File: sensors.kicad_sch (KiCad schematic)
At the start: 13 parts, among them U5 LIS2MDL, U6 SAM-M10Q

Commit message: modified BOM
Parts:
- C13, C17: Distributor Link https://www.lcsc.com/product-detail/C95841.html -> https://www.digikey.com/en/products/detail/samsung-electro-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
- C14, C15, C18, C23: Distributor Link https://www.lcsc.com/product-detail/C519980.html -> https://www.digikey.com/en/products/detail/samsung-electro-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; MPN CC0805KRX7R7BB104 -> CL21B104KBCNNNC; Manufacturer YAGEO -> Samsung Electro-Mechanics
- C16: Distributor Link https://www.lcsc.com/product-detail/C113853.html -> https://www.digikey.com/en/products/detail/samsung-electro-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; MPN CC0805KRX7R7BB224 -> CL21B224KAFNNNE; Manufacturer YAGEO -> Samsung Electro-Mechanics
- R14, R15: Distributor Link https://www.lcsc.com/product-detail/C17414.html -> https://www.digikey.com/en/products/detail/yageo/RC0805JR-0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; MPN 0805W8F1002T5E -> RC0805JR-0710KL; Manufacturer UNI-ROYAL -> YAGEO
- R16, R17: Distributor Link https://www.lcsc.com/product-detail/C17520.html -> https://www.digikey.com/en/products/detail/yageo/RC0805FR-0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; MPN 0805W8F2201T5E -> RC0805FR-072K2L; Manufacturer UNI-ROYAL -> YAGEO
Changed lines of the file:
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@@
 			)
 		)
-		(property "Datasheet" "https://www.lcsc.com/datasheet/C519980.pdf"
+		(property "Datasheet" ""
 			(at 182.88 59.69 0)
 			(effects
@@
 			)
 		)
-		(property "MPN" "CC0805KRX7R7BB104"
+		(property "MPN" "CL21B104KBCNNNC"
 			(at 182.88 59.69 0)
 			(effects
@@
 			)
 		)
-		(property "Manufacturer" "YAGEO"
+		(property "Manufacturer" "Samsung Electro-Mechanics"
 			(at 182.88 59.69 0)
 			(effects
@@
 			)
 		)
-		(property "Distributor Link" "https://www.lcsc.com/product-detail/C519980.html"
+		(property "Distributor Link" "https://www.digikey.com/en/products/detail/samsung-electro-mechanics/CL21B104KBCNNNC/3886661"
+			(at 182.88 59.69 0)
+			(effects
+				(font
+					(size 1.27 1.27)
+				)
+				(hide yes)
+			)
+		)
+		(property "DIGIKEY" ""
 			(at 182.88 59.69 0)
 			(effects
@@
 			)
 		)
+		(property "DIGIKEY" ""
+			(at 96.52 82.55 0)
+			(effects
+				(font
+					(size 1.27 1.27)
+				)
+				(hide yes)
+			)
+		)
 		(pin "3"
 		)
@@
 			)
 		)
-		(property "Datasheet" "https://www.lcsc.com/datasheet/C113853.pdf"
+		(property "Datasheet" ""
 			(at 119.38 92.71 0)
 			(effects
@@
 			)
 		)
-		(property "MPN" "CC0805KRX7R7BB224"
+		(property "MPN" "CL21B224KAFNNNE"
 			(at 119.38 92.71 0)
 			(effects
@@
 			)
 		)
-		(property "Manufacturer" "YAGEO"
+		(property "Manufacturer" "Samsung Electro-Mechanics"
 			(at 119.38 92.71 0)
 			(effects
@@
 			)
 		)
-		(property "Distributor Link" "https://www.lcsc.com/product-detail/C113853.html"
+		(property "Distributor Link" "https://www.digikey.com/en/products/detail/samsung-electro-mechanics/CL21B224KAFNNNE/3886819"
+			(at 119.38 92.71 0)
+			(effects
+				(font
+					(size 1.27 1.27)
+				)
+				(hide yes)
+			)
+		)
+		(property "DIGIKEY" ""
 			(at 119.38 92.71 0)
 			(effects
@@
 			)
 		)
-		(property "Datasheet" "https://www.lcsc.com/datasheet/C17520.pdf"
+		(property "Datasheet" ""
 			(at 218.44 78.74 0)
 			(effects
@@
 			)
 		)
-		(property "MPN" "0805W8F2201T5E"
+		(property "MPN" "RC0805FR-072K2L"
 			(at 218.44 78.74 90)
 			(effects
@@
 			)
 		)
-		(property "Manufacturer" "UNI-ROYAL"
+		(property "Manufacturer" "YAGEO"
 			(at 218.44 78.74 90)
 			(effects
@@
 			)
 		)
-		(property "Distributor Link" "https://www.lcsc.com/product-detail/C17520.html"
+		(property "Distributor Link" "https://www.digikey.com/en/products/detail/yageo/RC0805FR-072K2L/727676"
+			(at 218.44 78.74 90)
+			(effects
+				(font
+					(size 1.27 1.27)
+				)
+				(hide yes)
+			)
+		)
+		(property "DIGIKEY" ""
 			(at 218.44 78.74 90)
 			(effects
@@
 			)
 		)
-		(property "Datasheet" "https://www.lcsc.com/datasheet/C519980.pdf"
+		(property "Datasheet" ""
 			(at 80.01 60.96 0)
 			(effects
@@
 			)
 		)
-		(property "MPN" "CC0805KRX7R7BB104"
+		(property "MPN" "CL21B104KBCNNNC"
 			(at 80.01 60.96 0)
 			(effects
@@
 			)
 		)
-		(property "Manufacturer" "YAGEO"
+		(property "Manufacturer" "Samsung Electro-Mechanics"
 			(at 80.01 60.96 0)
 			(effects
@@
 			)
 		)
-		(property "Distributor Link" "https://www.lcsc.com/product-detail/C519980.html"
+		(property "Distributor Link" "https://www.digikey.com/en/products/detail/samsung-electro-mechanics/CL21B104KBCNNNC/3886661"
+			(at 80.01 60.96 0)
+			(effects
+				(font
+					(size 1.27 1.27)
+				)
+				(hide yes)
+			)
+		)
+		(property "DIGIKEY" ""
 			(at 80.01 60.96 0)
 			(effects
@@
 			)
 		)
-		(property "Datasheet" "https://www.lcsc.com/datasheet/C95841.pdf"
+		(property "Datasheet" ""
 			(at 158.75 59.69 0)
 			(effects
@@
 			)
 		)
-		(property "Distributor Link" "https://www.lcsc.com/product-detail/C95841.html"
+		(property "Distributor Link" "https://www.digikey.com/en/products/detail/samsung-electro-mechanics/CL21B106KOQNNNE/3888530"
+			(at 158.75 59.69 0)
+			(effects
+				(font
+					(size 1.27 1.27)
+				)
+				(hide yes)
+			)
+		)
+		(property "DIGIKEY" ""
 			(at 158.75 59.69 0)
 			(effects
@@
 			)
 		)
-		(property "Datasheet" "https://www.lcsc.com/datasheet/C17520.pdf"
+		(property "Datasheet" ""
 			(at 212.09 78.74 0)
 			(effects
@@
 			)
 		)
-		(property "MPN" "0805W8F2201T5E"
+		(property "MPN" "RC0805FR-072K2L"
 			(at 212.09 78.74 90)
 			(effects
@@
 			)
 		)
-		(property "Manufacturer" "UNI-ROYAL"
+		(property "Manufacturer" "YAGEO"
 			(at 212.09 78.74 90)
 			(effects
@@
 			)
 		)
-		(property "Distributor Link" "https://www.lcsc.com/product-detail/C17520.html"
+		(property "Distributor Link" "https://www.digikey.com/en/products/detail/yageo/RC0805FR-072K2L/727676"
+			(at 212.09 78.74 90)
+			(effects
+				(font
+					(size 1.27 1.27)
+				)
+				(hide yes)
+			)
+		)
+		(property "DIGIKEY" ""
 			(at 212.09 78.74 90)
 			(effects
@@
 			)
 		)
-		(property "Datasheet" "https://www.lcsc.com/datasheet/C17414.pdf"
+		(property "Datasheet" ""
 			(at 58.42 74.93 0)
 			(effects
@@
 			)
 		)
-		(property "MPN" "0805W8F1002T5E"
+		(property "MPN" "RC0805JR-0710KL"
 			(at 58.42 74.93 0)
 			(effects
@@
 			)
 		)
-		(property "Manufacturer" "UNI-ROYAL"
+		(property "Manufacturer" "YAGEO"
 			(at 58.42 74.93 0)
 			(effects
@@
 			)
 		)
-		(property "Distributor Link" "https://www.lcsc.com/product-detail/C17414.html"
+		(property "Distributor Link" "https://www.digikey.com/en/products/detail/yageo/RC0805JR-0710KL/728241"
+			(at 58.42 74.93 0)
+			(effects
+				(font
+					(size 1.27 1.27)
+				)
+				(hide yes)
+			)
+		)
+		(property "DIGIKEY" ""
 			(at 58.42 74.93 0)
 			(effects
@@
 			)
 		)
+		(property "DIGIKEY" ""
+			(at 191.77 81.28 0)
+			(effects
+				(font
+					(size 1.27 1.27)
+				)
+				(hide yes)
+			)
+		)
 		(pin "9"
 		)
@@
 			)
 		)
-		(property "Datasheet" "https://www.lcsc.com/datasheet/C519980.pdf"
+		(property "Datasheet" ""
 			(at 171.45 59.69 0)
 			(effects
@@
 			)
 		)
-		(property "MPN" "CC0805KRX7R7BB104"
+		(property "MPN" "CL21B104KBCNNNC"
 			(at 171.45 59.69 0)
 			(effects
@@
 			)
 		)
-		(property "Manufacturer" "YAGEO"
+		(property "Manufacturer" "Samsung Electro-Mechanics"
 			(at 171.45 59.69 0)
 			(effects
@@
 			)
 		)
-		(property "Distributor Link" "https://www.lcsc.com/product-detail/C519980.html"
+		(property "Distributor Link" "https://www.digikey.com/en/products/detail/samsung-electro-mechanics/CL21B104KBCNNNC/3886661"
+			(at 171.45 59.69 0)
+			(effects
+				(font
+					(size 1.27 1.27)
+				)
+				(hide yes)
+			)
+		)
+		(property "DIGIKEY" ""
 			(at 171.45 59.69 0)
 			(effects
@@
 			)
 		)
-		(property "Datasheet" "https://www.lcsc.com/datasheet/C17414.pdf"
+		(property "Datasheet" ""
 			(at 63.5 74.93 0)
 			(effects
@@
 			)
 		)
-		(property "MPN" "0805W8F1002T5E"
+		(property "MPN" "RC0805JR-0710KL"
 			(at 63.5 74.93 0)
 			(effects
@@
 			)
 		)
-		(property "Manufacturer" "UNI-ROYAL"
+		(property "Manufacturer" "YAGEO"
 			(at 63.5 74.93 0)
 			(effects
@@
 			)
 		)
-		(property "Distributor Link" "https://www.lcsc.com/product-detail/C17414.html"
+		(property "Distributor Link" "https://www.digikey.com/en/products/detail/yageo/RC0805JR-0710KL/728241"
+			(at 63.5 74.93 0)
+			(effects
+				(font
+					(size 1.27 1.27)
+				)
+				(hide yes)
+			)
+		)
+		(property "DIGIKEY" ""
 			(at 63.5 74.93 0)
 			(effects
@@
 			)
 		)
-		(property "Datasheet" "https://www.lcsc.com/datasheet/C519980.pdf"
+		(property "Datasheet" ""
 			(at 92.71 60.96 0)
 			(effects
@@
 			)
 		)
-		(property "MPN" "CC0805KRX7R7BB104"
+		(property "MPN" "CL21B104KBCNNNC"
 			(at 92.71 60.96 0)
 			(effects
@@
 			)
 		)
-		(property "Manufacturer" "YAGEO"
+		(property "Manufacturer" "Samsung Electro-Mechanics"
 			(at 92.71 60.96 0)
 			(effects
@@
 			)
 		)
-		(property "Distributor Link" "https://www.lcsc.com/product-detail/C519980.html"
+		(property "Distributor Link" "https://www.digikey.com/en/products/detail/samsung-electro-mechanics/CL21B104KBCNNNC/3886661"
+			(at 92.71 60.96 0)
+			(effects
+				(font
+					(size 1.27 1.27)
+				)
+				(hide yes)
+			)
+		)
+		(property "DIGIKEY" ""
 			(at 92.71 60.96 0)
 			(effects
@@
 			)
 		)
-		(property "Datasheet" "https://www.lcsc.com/datasheet/C95841.pdf"
+		(property "Datasheet" ""
 			(at 67.31 60.96 0)
 			(effects
@@
 			)
 		)
-		(property "Distributor Link" "https://www.lcsc.com/product-detail/C95841.html"
+		(property "Distributor Link" "https://www.digikey.com/en/products/detail/samsung-electro-mechanics/CL21B106KOQNNNE/3888530"
 			(at 67.31 60.96 0)
 			(effects
+				(font
+					(size 1.27 1.27)
+				)
+				(hide yes)
+			)
+		)
+		(property "DIGIKEY" ""
+			(at 67.31 60.96 0)
+			(effects

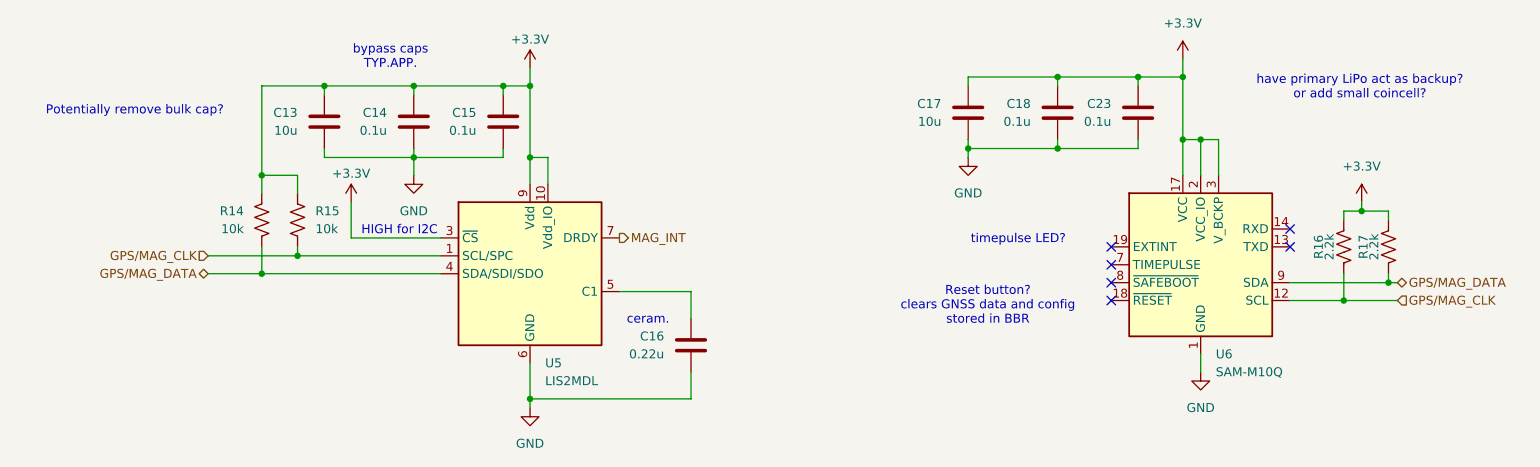
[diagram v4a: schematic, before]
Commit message: modified battery terminal
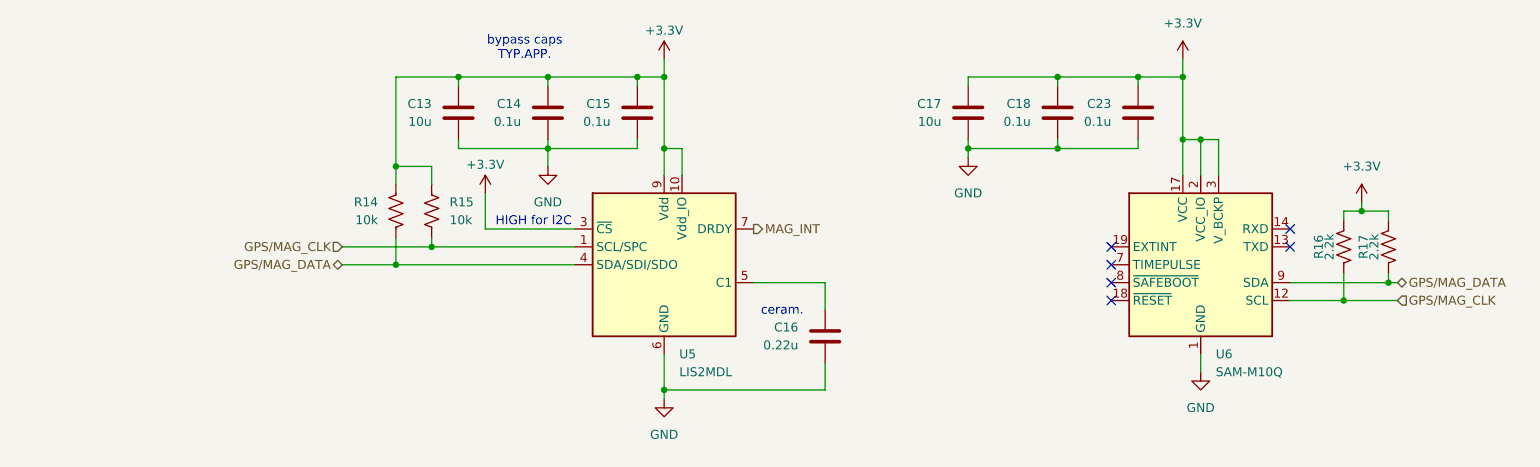
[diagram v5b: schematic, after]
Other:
- note removed: "Potentially remove bulk cap?"
- note removed: "Reset button? clears GNSS data and config stored in BBR"
- note removed: "have primary LiPo act as backup? or add small coincell?"
- note removed: "timepulse LED?"
- moved on the sheet: C13, C14, C15, C16, R14, R15, U5

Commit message: REV 1.0 Ordered
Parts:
- renumbered C23 to C19
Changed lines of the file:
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@@
 		(dnp no)
 		(fields_autoplaced yes)
-		(property "Reference" "#PWR033"
+		(property "Reference" "#PWR035"
 			(at 189.23 55.88 0)
 			(effects
@@
 			(project "ESP32_Tracker"
 				(path "/92195c42-0bc4-473e-a890-6f85786d3c69/df595db4-adad-4efb-b42f-768fb30b12a2"
-					(reference "#PWR033")
+					(reference "#PWR035")
 					(unit 1)
 				)
@@
 		(on_board yes)
 		(dnp no)
-		(property "Reference" "C23"
+		(property "Reference" "C19"
 			(at 179.07 58.4199 0)
 			(effects
@@
 			(project "ESP32_Tracker"
 				(path "/92195c42-0bc4-473e-a890-6f85786d3c69/df595db4-adad-4efb-b42f-768fb30b12a2"
-					(reference "C23")
+					(reference "C19")
 					(unit 1)
 				)
@@
 		(dnp no)
 		(fields_autoplaced yes)
-		(property "Reference" "#PWR035"
+		(property "Reference" "#PWR037"
 			(at 214.63 76.2 0)
 			(effects
@@
 			(project "ESP32_Tracker"
 				(path "/92195c42-0bc4-473e-a890-6f85786d3c69/df595db4-adad-4efb-b42f-768fb30b12a2"
-					(reference "#PWR035")
+					(reference "#PWR037")
 					(unit 1)
 				)
@@
 		(on_board yes)
 		(dnp no)
-		(property "Reference" "#PWR04"
+		(property "Reference" "#PWR030"
 			(at 90.17 74.93 0)
 			(effects
@@
 			(project "ESP32_Tracker"
 				(path "/92195c42-0bc4-473e-a890-6f85786d3c69/df595db4-adad-4efb-b42f-768fb30b12a2"
-					(reference "#PWR04")
+					(reference "#PWR030")
 					(unit 1)
 				)
@@
 		(dnp no)
 		(fields_autoplaced yes)
-		(property "Reference" "#PWR031"
+		(property "Reference" "#PWR033"
 			(at 115.57 106.68 0)
 			(effects
@@
 			(project "ESP32_Tracker"
 				(path "/92195c42-0bc4-473e-a890-6f85786d3c69/df595db4-adad-4efb-b42f-768fb30b12a2"
-					(reference "#PWR031")
+					(reference "#PWR033")
 					(unit 1)
 				)
@@
 		(dnp no)
 		(fields_autoplaced yes)
-		(property "Reference" "#PWR032"
+		(property "Reference" "#PWR034"
 			(at 158.75 72.39 0)
 			(effects
@@
 			(project "ESP32_Tracker"
 				(path "/92195c42-0bc4-473e-a890-6f85786d3c69/df595db4-adad-4efb-b42f-768fb30b12a2"
-					(reference "#PWR032")
+					(reference "#PWR034")
 					(unit 1)
 				)
@@
 		(dnp no)
 		(fields_autoplaced yes)
-		(property "Reference" "#PWR034"
+		(property "Reference" "#PWR036"
 			(at 191.77 102.87 0)
 			(effects
@@
 			(project "ESP32_Tracker"
 				(path "/92195c42-0bc4-473e-a890-6f85786d3c69/df595db4-adad-4efb-b42f-768fb30b12a2"
-					(reference "#PWR034")
+					(reference "#PWR036")
 					(unit 1)
 				)
@@
 		(dnp no)
 		(fields_autoplaced yes)
-		(property "Reference" "#PWR029"
+		(property "Reference" "#PWR031"
 			(at 99.06 73.66 0)
 			(effects
@@
 			(project "ESP32_Tracker"
 				(path "/92195c42-0bc4-473e-a890-6f85786d3c69/df595db4-adad-4efb-b42f-768fb30b12a2"
-					(reference "#PWR029")
+					(reference "#PWR031")
 					(unit 1)
 				)
@@
 		(on_board yes)
 		(dnp no)
-		(property "Reference" "#PWR030"
+		(property "Reference" "#PWR032"
 			(at 115.57 55.88 0)
 			(effects
@@
 			(project "ESP32_Tracker"
 				(path "/92195c42-0bc4-473e-a890-6f85786d3c69/df595db4-adad-4efb-b42f-768fb30b12a2"
-					(reference "#PWR030")
-					(unit 1)
-				)
+					(reference "#PWR032")
+					(unit 1)
+				)
